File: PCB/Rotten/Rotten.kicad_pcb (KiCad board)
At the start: 2 copper layers, 39 parts, among them J1 Jack-DC, J2 FOOTSWITCH, J3 JACK OUTPUT, J4 JACK INPUT, Q1 2N5458, U1 AS301

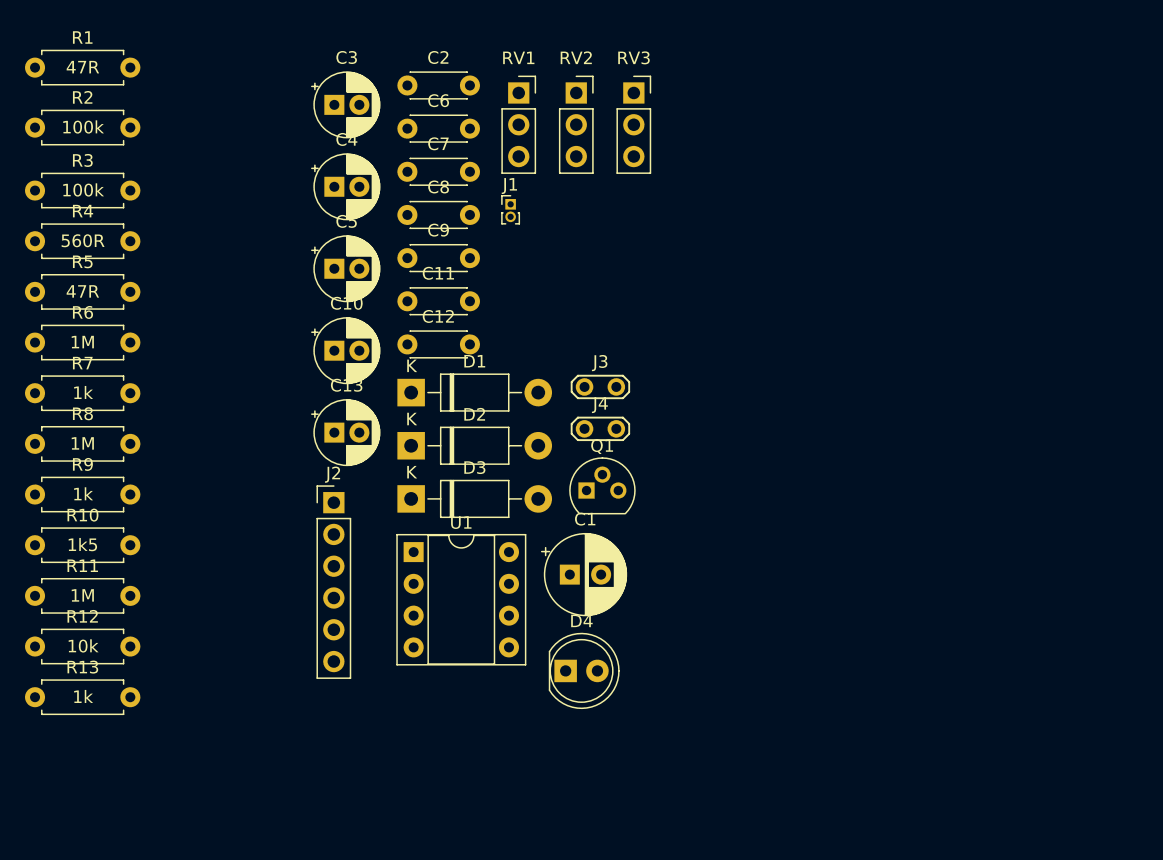
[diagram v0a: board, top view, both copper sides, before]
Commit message: created rev1 layout and added images
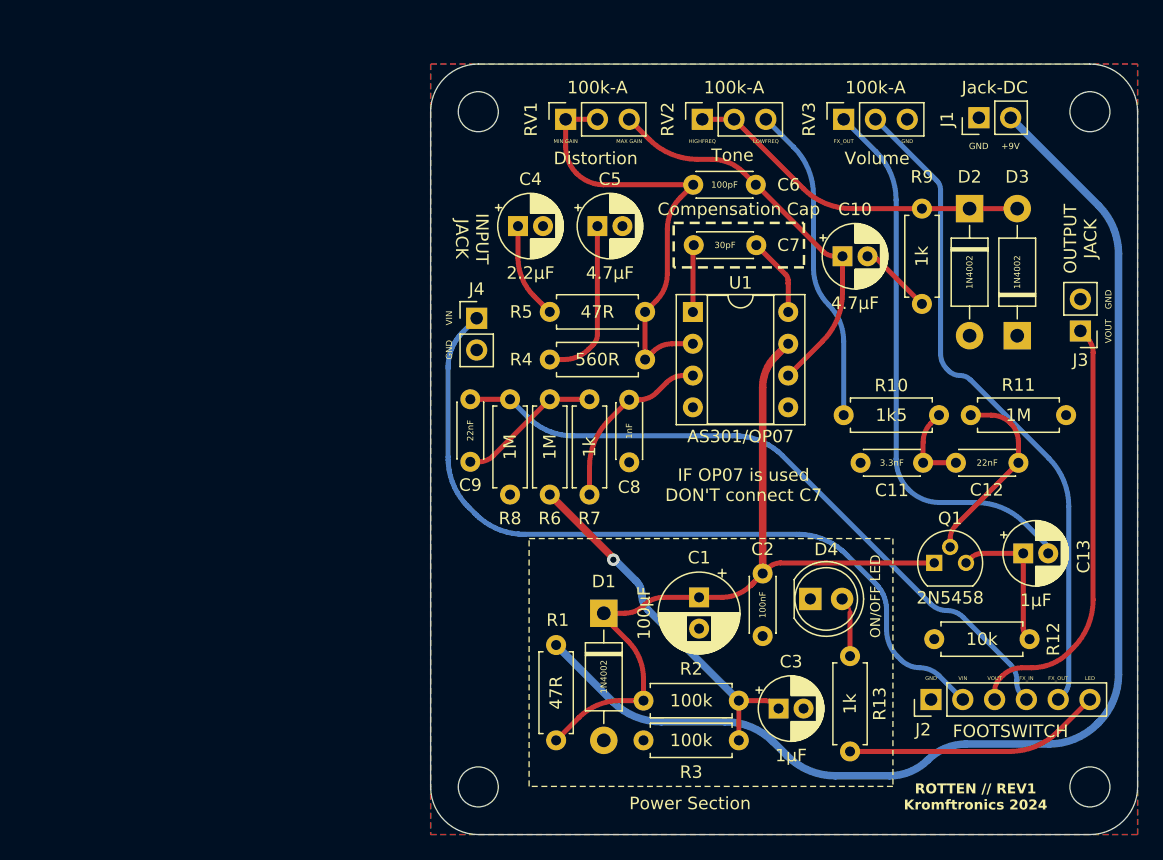
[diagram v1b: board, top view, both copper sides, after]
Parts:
- added H1: MountingHole, MountingHole:MountingHole_3.2mm_M3_DIN965, F.Cu at (97.2, 58.4)
- added H2: MountingHole, MountingHole:MountingHole_3.2mm_M3_DIN965, F.Cu at (146.1, 58.4)
- added H3: MountingHole, MountingHole:MountingHole_3.2mm_M3_DIN965, F.Cu at (97.2, 112.4)
- added H4: MountingHole, MountingHole:MountingHole_3.2mm_M3_DIN965, F.Cu at (146.1, 112.4)
- D4: value LED -> ON/OFF LED
- J1: footprint Connector_PinHeader_1.00mm:PinHeader_1x02_P1.00mm_Vertical -> Connector_PinHeader_2.54mm:PinHeader_1x02_P2.54mm_Vertical
- J3, J4: footprint TestPoint:TestPoint_2Pads_Pitch2.54mm_Drill0.8mm -> Connector_PinHeader_2.54mm:PinHeader_1x02_P2.54mm_Vertical
- U1: value AS301 -> AS301/OP07
- moved R11 83.7 mm to (144.1, 82.7), turned to 180 degrees
- moved R2 72.6 mm to (118.0, 105.5), turned to 180 degrees
- moved R9 72.5 mm to (132.6, 73.8), turned to 90 degrees
- moved R12 71.9 mm to (133.6, 100.6)
- moved R3 65.6 mm to (110.4, 108.7)
- moved R10 65.5 mm to (126.4, 82.7)
- moved R13 65.2 mm to (126.9, 101.9), turned to -90 degrees
- moved R1 62.2 mm to (103.4, 101.1), turned to -90 degrees
- moved C3 59.9 mm to (121.2, 106.1)
- moved C13 55.9 mm to (140.7, 93.7)
- moved J2 50.3 mm to (133.3, 105.4), turned to 90 degrees
- moved D3 50.2 mm to (140.2, 76.3), turned to 90 degrees
- moved D2 48.5 mm to (136.4, 66.2), turned to -90 degrees
- moved C2 48.3 mm to (119.9, 95.3), turned to -90 degrees
- moved C12 44.9 mm to (135.3, 86.5)
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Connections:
- J3 pad 1: (no net) -> /VOUT
- J3 pad 2: (no net) -> GND
- J4 pad 1: (no net) -> /VIN
- J4 pad 2: (no net) -> GND
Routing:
- net /+9V_IN: track 0.00 -> 100.1 mm
- net /VIN: track 0.00 -> 63.6 mm
- net +9V: track 0.00 -> 62.8 mm
- net /FX_IN: track 0.00 -> 54.5 mm
- net /FX_OUT: track 0.00 -> 53.1 mm
- net Net-(C13-Pad2): track 0.00 -> 44.4 mm
- net Net-(U1--): track 0.00 -> 35.6 mm
- net /VOUT: track 0.00 -> 34.4 mm
- net Net-(C10-Pad1): track 0.00 -> 31.9 mm
- net /+4V5: track 0.00 -> 29.2 mm, vias 0 -> 1
- net Net-(D2-K): track 0.00 -> 27.9 mm
- net Net-(R10-Pad1): track 0.00 -> 25.6 mm
- net /LED: track 0.00 -> 20.6 mm
- net Net-(Q1-G): track 0.00 -> 15.6 mm
- net Net-(U1-+): track 0.00 -> 14.3 mm
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- added copper zone on B.Cu, net GND
- added copper zone on F.Cu, net GND
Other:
- board outline added: 56.5 x 61.6 mm
- board text added: "+9V"
- board text added: "Compensation Cap"
- board text added: "Distortion"
- board text added: "FX_IN"
- board text added: "FX_OUT"
- board text added: "GND"
- board text added: "HIGHFREQ"
- board text added: "IF OP07 is used DON'T connect C7"
- board text added: "INPUT JACK"
- board text added: "LED"
- board text added: "LOWFREQ"
- board text added: "MAX GAIN"
- board text added: "MIN GAIN"
- board text added: "OUTPUT JACK"
- board text added: "Power Section"
- board text added: "ROTTEN // REV1 Kromftronics 2024"
- board text added: "Tone"
- board text added: "VIN"
- board text added: "VOUT"
- board text added: "Volume"
